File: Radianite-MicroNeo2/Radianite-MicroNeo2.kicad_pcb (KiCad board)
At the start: 4 copper layers, 50 x 33 mm, 87 parts, among them J1 Micro_SD_Card_Det1, J2 USB_C_Receptacle_USB2.0_16P, J3 USB_C_Receptacle_USB2.0_16P, J4 AudioJack4, J6 Conn_02x16_Odd_Even, SW1 SW_Push, SW2 SW_SPDT, U1 F1C200s, U3 CH340E, U4 W25Q32JVZP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

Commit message: fix more stuffs
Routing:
- net GND: vias 218 -> 233

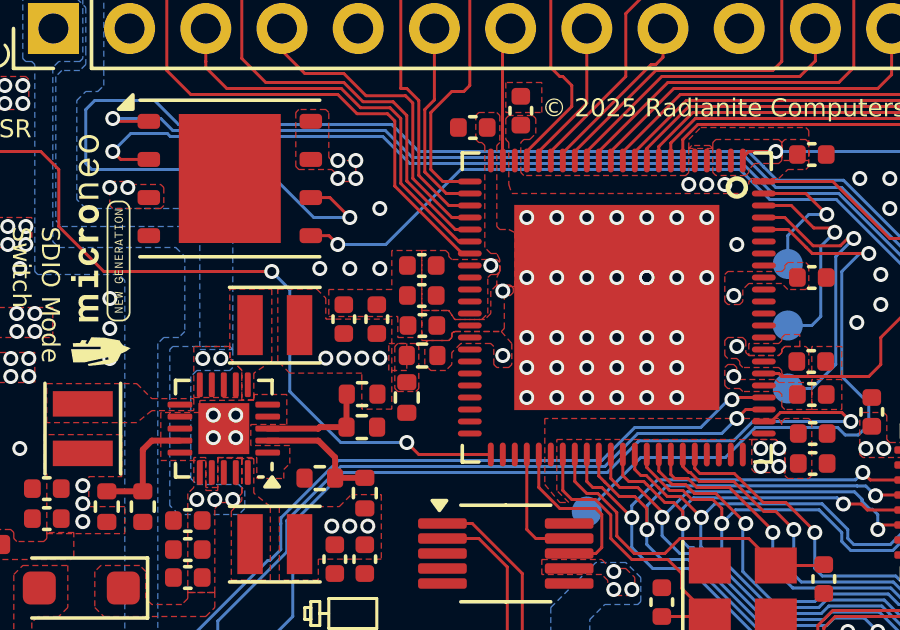
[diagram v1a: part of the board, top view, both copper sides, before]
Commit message: turns out SVREF is a divided voltage between DRAM
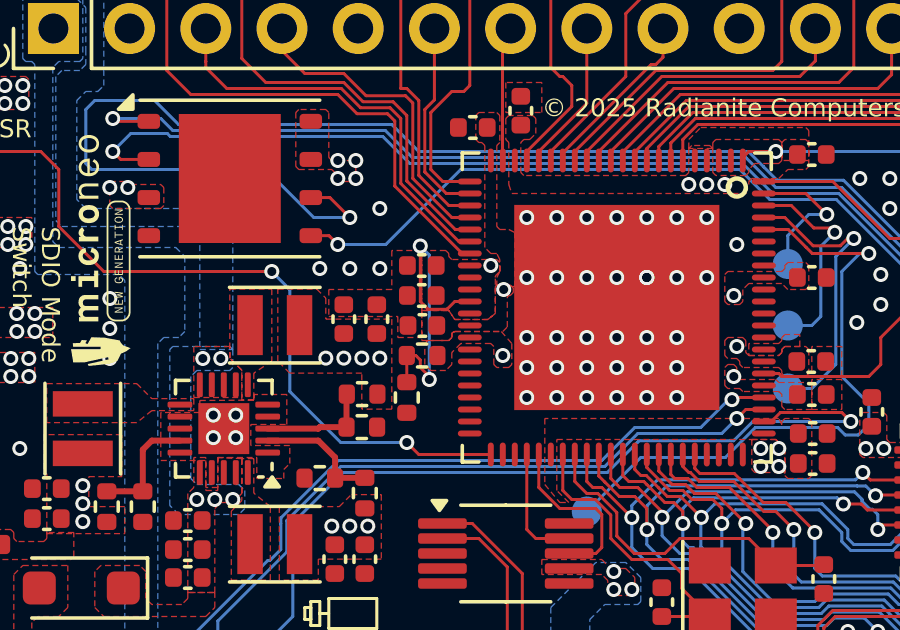
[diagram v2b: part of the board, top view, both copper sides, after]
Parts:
- turned R8 to 180 degrees
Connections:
- R8 pad 2: VRAM -> Net-(U1B-SVREF)
- R9 pad 2: VRAM -> Net-(U1B-SVREF)
- U1 pad 33: VRAM -> Net-(U1B-SVREF)
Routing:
- net Net-(U1B-SVREF): track 0.00 -> 10.5 mm, vias 0 -> 2
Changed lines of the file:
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@@
 	(net 121 "Net-(J2-CC2)")
 	(net 122 "unconnected-(J2-SBU1-PadA8)")
+	(net 123 "Net-(U1B-SVREF)")
 	(footprint "Inductor_SMD:L_Changjiang_FNR252010S"
 		(layer "F.Cu")
@@
 			(zone_connect 2)
 		)
-		(model "${KICAD8_3DMODEL_DIR}/Package_DFN_QFN.3dshapes/WQFN-20-1EP_3x3mm_P0.4mm_EP1.7x1.7mm.wrl"
+		(model "${KICAD8_3DMODEL_DIR}/Package_DFN_QFN.3dshapes/QFN-20-1EP_4x4mm_P0.5mm.step"
 			(offset
 				(xyz 0 0 0)
 			)
 			(scale
-				(xyz 1 1 1)
+				(xyz 0.8 0.8 0.8)
 			)
 			(rotate
@@
 			(size 0.2 0.8)
 			(layers "F.Cu" "F.Paste" "F.Mask")
-			(net 4 "VRAM")
+			(net 123 "Net-(U1B-SVREF)")
 			(pinfunction "SVREF")
 			(pintype "input")
@@
 			(layers "F.Cu" "F.Paste" "F.Mask")
 			(roundrect_rratio 0.25)
-			(net 4 "VRAM")
+			(net 123 "Net-(U1B-SVREF)")
 			(pintype "passive")
 		)
@@
 	(footprint "Resistor_SMD:R_0402_1005Metric"
 		(layer "F.Cu")
-		(at 98.41 71.9)
+		(at 98.41 71.9 180)
 		(descr "Resistor SMD 0402 (1005 Metric), square (rectangular) end terminal, IPC_7351 nominal, (Body size source: IPC-SM-782 page 72, https://www.pcb-3d.com/wordpress/wp-content/uploads/ipc-sm-782a_amendment_1_and_2.pdf), generated with kicad-footprint-generator")
 		(tags "resistor")
 		(property "Reference" "R8"
-			(at 0 -1.17 0)
+			(at 0 -1.17 360)
 			(layer "F.SilkS")
 			(hide yes)
@@
 		)
 		(property "Value" "2.2k"
-			(at 0 1.17 0)
+			(at 0 1.17 360)
 			(layer "F.Fab")
 			(effects
@@
 		)
 		(property "Footprint" "Resistor_SMD:R_0402_1005Metric"
-			(at 0 0 0)
+			(at 0 0 180)
 			(unlocked yes)
 			(layer "F.Fab")
@@
 		)
 		(property "Datasheet" ""
-			(at 0 0 0)
+			(at 0 0 180)
 			(unlocked yes)
 			(layer "F.Fab")
@@
 		)
 		(property "Description" "Resistor"
-			(at 0 0 0)
+			(at 0 0 180)
 			(unlocked yes)
 			(layer "F.Fab")
@@
 		(attr smd)
 		(fp_line
-			(start -0.153641 -0.38)
-			(end 0.153641 -0.38)
+			(start -0.153641 0.38)
+			(end 0.153641 0.38)
 			(stroke
 				(width 0.12)
@@
 		)
 		(fp_line
-			(start -0.153641 0.38)
-			(end 0.153641 0.38)
+			(start -0.153641 -0.38)
+			(end 0.153641 -0.38)
 			(stroke
 				(width 0.12)
@@
 		)
 		(fp_line
-			(start -0.93 -0.47)
-			(end 0.93 -0.47)
+			(start 0.93 0.47)
+			(end -0.93 0.47)
 			(stroke
 				(width 0.05)
@@
 		)
 		(fp_line
-			(start -0.93 0.47)
-			(end -0.93 -0.47)
+			(start 0.93 -0.47)
+			(end 0.93 0.47)
 			(stroke
 				(width 0.05)
@@
 		)
 		(fp_line
-			(start 0.93 -0.47)
-			(end 0.93 0.47)
+			(start -0.93 0.47)
+			(end -0.93 -0.47)
 			(stroke
 				(width 0.05)
@@
 		)
 		(fp_line
-			(start 0.93 0.47)
-			(end -0.93 0.47)
+			(start -0.93 -0.47)
+			(end 0.93 -0.47)
 			(stroke
 				(width 0.05)
@@
 		)
 		(fp_line
-			(start -0.525 -0.27)
-			(end 0.525 -0.27)
+			(start 0.525 0.27)
+			(end -0.525 0.27)
 			(stroke
 				(width 0.1)
@@
 		)
 		(fp_line
-			(start -0.525 0.27)
-			(end -0.525 -0.27)
+			(start 0.525 -0.27)
+			(end 0.525 0.27)
 			(stroke
 				(width 0.1)
@@
 		)
 		(fp_line
-			(start 0.525 -0.27)
-			(end 0.525 0.27)
+			(start -0.525 0.27)
+			(end -0.525 -0.27)
 			(stroke
 				(width 0.1)
@@
 		)
 		(fp_line
-			(start 0.525 0.27)
-			(end -0.525 0.27)
+			(start -0.525 -0.27)
+			(end 0.525 -0.27)
 			(stroke
 				(width 0.1)
@@
 		)
 		(fp_text user "${REFERENCE}"
-			(at 0 0 0)
+			(at 0 0 360)
 			(layer "F.Fab")
 			(effects
@@
 		)
 		(pad "1" smd roundrect
-			(at -0.51 0)
+			(at -0.509999 0 180)
 			(size 0.54 0.64)
 			(layers "F.Cu" "F.Paste" "F.Mask")
@@
 		)
 		(pad "2" smd roundrect
-			(at 0.51 0)
+			(at 0.509999 0 180)
 			(size 0.54 0.64)
 			(layers "F.Cu" "F.Paste" "F.Mask")
 			(roundrect_rratio 0.25)
-			(net 4 "VRAM")
+			(net 123 "Net-(U1B-SVREF)")
 			(pintype "passive")
 		)
@@
 	)
 	(via
-		(at 101.1 69.75)
+		(at 101.129998 69.7)
 		(size 0.5)
 		(drill 0.3)
@@
 		(net 121)
 	)
+	(segment
+		(start 98.35 70.1)
+		(end 98.35 68.25)
+		(width 0.1)
+		(layer "F.Cu")
+		(net 123)
+	)
+	(segment
+		(start 98.65 72.6)
+		(end 98.65 72.7)
+		(width 0.1)
+		(layer "F.Cu")
+		(net 123)
+	)
+	(segment
+		(start 99.25 70.35)
+		(end 99.24 70.36)
+		(width 0.1)
+		(layer "F.Cu")
+		(net 123)
+	)
+	(segment
+		(start 99.24 70.36)
+		(end 98.61 70.36)
+		(width 0.1)
+		(layer "F.Cu")
+		(net 123)
+	)
+	(segment
+		(start 100 70.1)
+		(end 99.5 70.1)
+		(width 0.1)
+		(layer "F.Cu")
+		(net 123)
+	)
+	(segment
+		(start 98.2 71.9)
+		(end 98.35 72.05)
+		(width 0.1)
+		(layer "F.Cu")
+		(net 123)
+	)
+	(segment
+		(start 97.900001 71.9)
+		(end 97.900001 72.79)
+		(width 0.1)
+		(layer "F.Cu")
+		(net 123)
+	)
+	(segment
+		(start 98.35 72.3)
+		(end 98.65 72.6)
+		(width 0.1)
+		(layer "F.Cu")
+		(net 123)
+	)
+	(segment
+		(start 98.35 72.05)
+		(end 98.35 72.3)
+		(width 0.1)
+		(layer "F.Cu")
+		(net 123)
+	)
+	(segment
+		(start 98.61 70.36)
+		(end 98.45 70.2)
+		(width 0.1)
+		(layer "F.Cu")
+		(net 123)
+	)
+	(segment
+		(start 97.900001 71.9)
+		(end 98.2 71.9)
+		(width 0.1)
+		(layer "F.Cu")
+		(net 123)
+	)
+	(segment
+		(start 98.45 70.2)
+		(end 98.35 70.1)
+		(width 0.1)
+		(layer "F.Cu")
+		(net 123)
+	)
+	(segment
+		(start 99.5 70.1)
+		(end 99.25 70.35)
+		(width 0.1)
+		(layer "F.Cu")
+		(net 123)
+	)
+	(segment
+		(start 97.900001 72.79)
+		(end 97.9 72.790001)
+		(width 0.1)
+		(layer "F.Cu")
+		(net 123)
+	)
+	(via
+		(at 98.65 72.7)
+		(size 0.5)
+		(drill 0.3)
+		(layers "F.Cu" "B.Cu")
+		(net 123)
+	)
+	(via
+		(at 98.35 68.25)
+		(size 0.5)
+		(drill 0.3)
+		(layers "F.Cu" "B.Cu")
+		(net 123)
+	)
+	(segment
+		(start 98.65 68.55)
+		(end 98.35 68.25)
+		(width 0.1)
+		(layer "B.Cu")
+		(net 123)
+	)
+	(segment
+		(start 98.65 72.7)
+		(end 98.65 68.55)
+		(width 0.1)
+		(layer "B.Cu")
+		(net 123)
+	)
 	(zone
 		(net 0)
@@
 			(pts
 				(xy 99.4 68.7) (xy 99.3 68.6) (xy 99.3 68.5) (xy 99.2 68.4) (xy 98.4 68.4) (xy 98.4 70.4) (xy 99.3 70.4)
-				(xy 99.5 70.7) (xy 100.4 70.7) (xy 100.6 70.5) (xy 100.6 69.3) (xy 100.7 69.2) (xy 100.9 69.2) (xy 101 69.1)
-				(xy 101 68.8) (xy 100.9 68.7)
+				(xy 99.5 70.7) (xy 100.6 70.7) (xy 100.85 70.5) (xy 100.85 69.3) (xy 100.85 69.25) (xy 100.9 69.2)
+				(xy 101 69.1) (xy 101 68.8) (xy 100.9 68.7)
 			)
 		)
@@
 	)
 	(zone
-		(net 4)
-		(net_name "VRAM")
-		(layer "F.Cu")
-		(hatch edge 0.5)
-		(priority 59)
-		(connect_pads yes
-			(clearance 0.05)
-		)
-		(min_thickness 0.25)
-		(filled_areas_thickness no)
-		(fill yes
-			(thermal_gap 0.5)
-			(thermal_bridge_width 0.5)
-		)
-		(polygon
-			(pts
-				(xy 97.3 71.5) (xy 97.9 71.5) (xy 97.9 72.4) (xy 97.3 72.4)
-			)
-		)
-	)
-	(zone
 		(net 3)
 		(net_name "+3V3")
@@
 	)
 	(zone
-		(net 4)
-		(net_name "VRAM")
-		(layer "F.Cu")
-		(hatch edge 0.5)
-		(priority 24)
-		(connect_pads yes
-			(clearance 0.125)
-		)
-		(min_thickness 0.25)
-		(filled_areas_thickness no)
-		(fill yes
-			(thermal_gap 0.5)
-			(thermal_bridge_width 0.5)
-		)
-		(polygon
-			(pts
-				(xy 97.5 73) (xy 97.6 73.1) (xy 98.2 73.1) (xy 98.3 73) (xy 98.3 71.6) (xy 98.2 71.5) (xy 97.6 71.5)
-				(xy 97.5 71.6)
-			)
-		)
-	)
-	(zone
 		(net 2)
 		(net_name "GND")
@@
 		(polygon
 			(pts
-				(xy 98.4 70.4) (xy 98.4 71.4) (xy 99.3 71.4) (xy 99.4 71.3) (xy 99.4 71.15) (xy 99.5 71.1) (xy 101.05 71.1)
-				(xy 101.15 71) (xy 101.15 70) (xy 101.25 69.9) (xy 101.35 69.9) (xy 101.45 69.8) (xy 101.45 69.65)
-				(xy 101.35 69.55) (xy 100.9 69.55) (xy 100.7 69.75) (xy 100.7 70.5) (xy 100.5 70.7) (xy 99.5 70.7)
+				(xy 98.4 70.4) (xy 98.4 71.4) (xy 99.3 71.4) (xy 99.4 71.3) (xy 99.4 71.15) (xy 99.5 71.1) (xy 101.1 71.1)
+				(xy 101.25 70.95) (xy 101.25 69.95) (xy 101.3 69.9) (xy 101.35 69.9) (xy 101.45 69.8) (xy 101.45 69.65)
+				(xy 101.35 69.55) (xy 100.9 69.55) (xy 100.85 69.6) (xy 100.85 70.5) (xy 100.6 70.7) (xy 99.5 70.7)
 				(xy 99.3 70.4)
 			)
